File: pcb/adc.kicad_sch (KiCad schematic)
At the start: 4 parts, among them U7 ADS1220

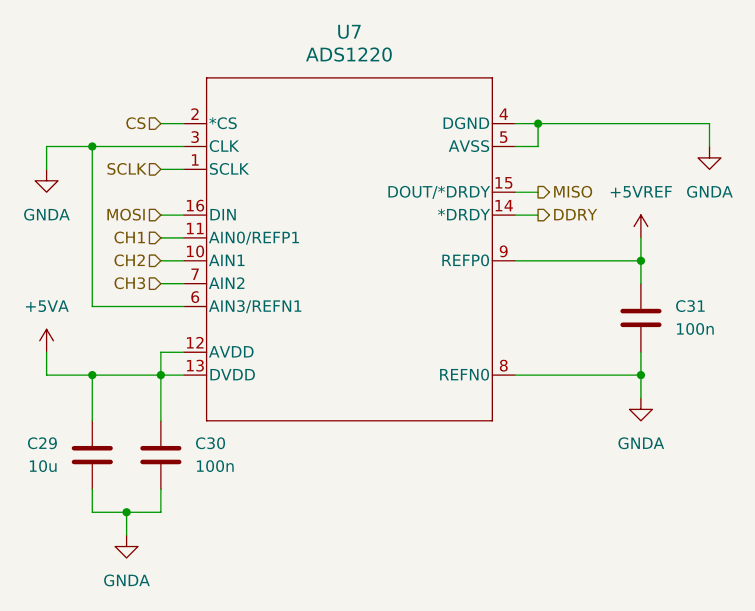
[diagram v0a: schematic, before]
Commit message: rework to tia feedback selection, board power, and ui
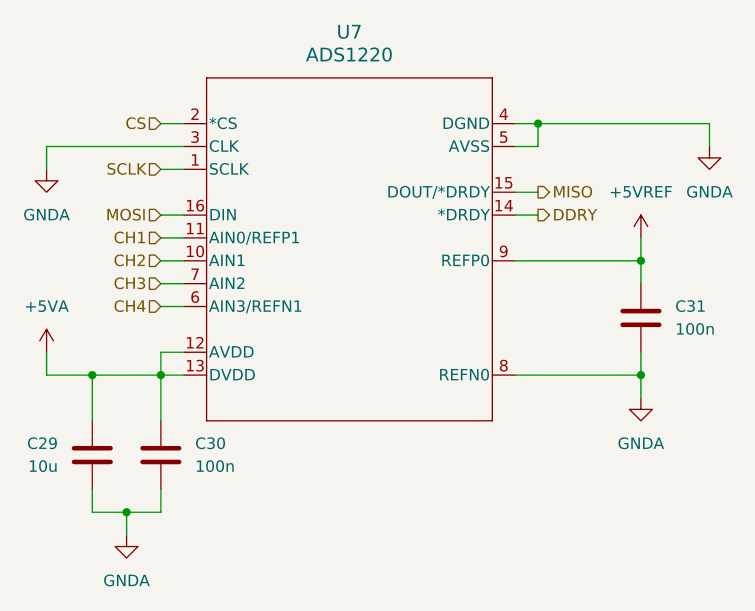
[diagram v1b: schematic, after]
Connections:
- net GNDA: no longer U7.6 (AIN3/REFN1)
- new net CH4: U7.6 (AIN3/REFN1)
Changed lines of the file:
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@@
-	)
-	(junction
-		(at 120.65 88.9)
-		(diameter 0)
-		(color 0 0 0 0)
 	)
 	(junction
@@
 	(wire
 		(pts
-			(xy 120.65 88.9) (xy 120.65 106.68)
-		)
-		(stroke
-			(width 0)
-			(type default)
-		)
-	)
-	(wire
-		(pts
-			(xy 120.65 88.9) (xy 115.57 88.9)
+			(xy 115.57 88.9) (xy 130.81 88.9)
 		)
 		(stroke
@@
 	(wire
 		(pts
-			(xy 130.81 88.9) (xy 120.65 88.9)
-		)
-		(stroke
-			(width 0)
-			(type default)
-		)
-	)
-	(wire
-		(pts
 			(xy 128.27 86.36) (xy 130.81 86.36)
 		)
@@
 	(wire
 		(pts
+			(xy 128.27 106.68) (xy 130.81 106.68)
+		)
+		(stroke
+			(width 0)
+			(type default)
+		)
+	)
+	(wire
+		(pts
 			(xy 124.46 129.54) (xy 124.46 132.08)
 		)
@@
 		(pts
 			(xy 128.27 101.6) (xy 130.81 101.6)
-		)
-		(stroke
-			(width 0)
-			(type default)
-		)
-	)
-	(wire
-		(pts
-			(xy 130.81 106.68) (xy 120.65 106.68)
 		)
 		(stroke
@@
 		)
 	)
+	(hierarchical_label "CH4"
+		(shape input)
+		(at 128.27 106.68 180)
+		(effects
+			(font
+				(size 1.27 1.27)
+			)
+			(justify right)
+		)
+	)
